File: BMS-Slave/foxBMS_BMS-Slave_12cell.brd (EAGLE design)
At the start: 160 x 100 mm, 371 parts, among them IC1001 ADG728BRUZ, IC1002 ADG728BRUZ, IC1003 LTC6255CS6, IC1004 LTC6255CS6, IC1005 ADG728BRUZ, IC1101 PCA8574TS, IC1201 PCA8574TS, IC1301 24AA02UID, IC1302 MCP9800A0T-M/OT, IC1401 24AA02UID, IC1402 MCP9800A0T-M/OT, IC201 0_LES_BATTERIE-MANAGEMENT.SMD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, IC301 0_LES_BATTERIE-MANAGEMENT.SMD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, IC801 ACPL-247-500E, IC802 ACPL-247-500E, IC803 ACPL-247-500E, IC901 ADG728BRUZ, IC902 ADG728BRUZ, IC903 LTC6255CS6, IC904 LTC6255CS6, IC905 ADG728BRUZ, T201 PBHV8115Z, T301 PBHV8115Z, T701 NX2301P, T702 NX2301P, T703 NX2301P, T704 NX2301P, T705 NX2301P, T706 NX2301P, T707 NX2301P, T708 NX2301P, T709 NX2301P, T710 NX2301P, T711 NX2301P, T712 NX2301P, X1501 MA09-2, X1502 MA09-2, X1503 43045-2400_MOLEX_24PIN, X1504 MA05-2, X1505 MA05-2, X1506 43045-1600_MOLEX_16PIN, X1507 43045-1600_MOLEX_16PIN, X1508 MA10-2, X1509 43045-0200_MOLEX_2PIN, X1510 43045-0200_MOLEX_2PIN, X1511 43045-0200_MOLEX_2PIN, X1512 43045-0200_MOLEX_2PIN

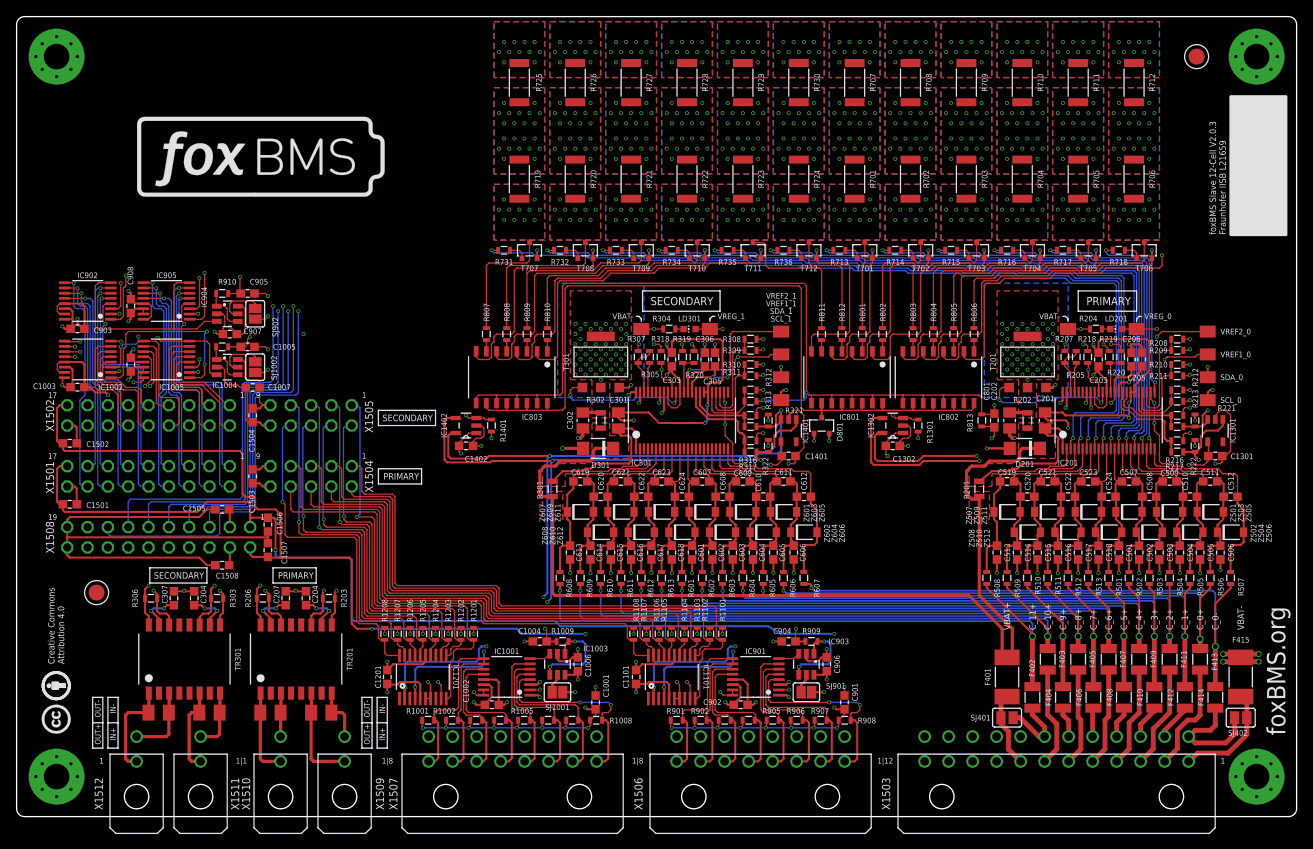
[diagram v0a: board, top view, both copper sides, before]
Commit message: updated foxBMS-slave to version 2.1.0
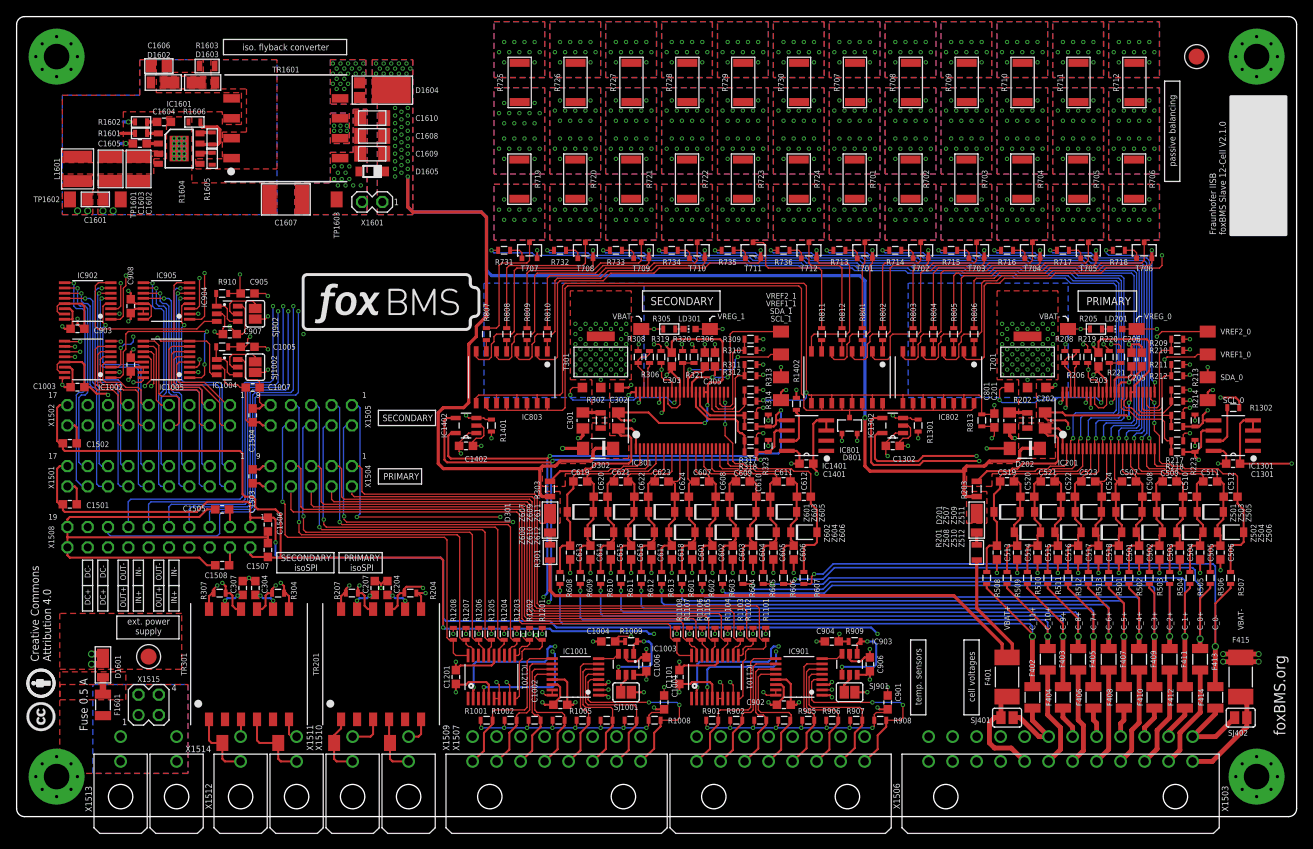
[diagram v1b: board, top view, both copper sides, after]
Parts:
- removed TP202, TP208, TP302, TP308: CUSTOM_PAD_PAD_2.0X1.5MM, foxBMS_BMS-Slave_12cell:CUSTOM_PAD_PAD2.0X1.5MM
- added C1601: 1,00µF_0805_25V_X7R_KEMET, 0_LES_KAPAZITAET.SMD.MLCC:C_SMD_0805_(2012)_R_KEMET_REV01
- added C1602, C1603: 10µF_1210_25V_X7R, 0_LES_KAPAZITAET.SMD.MLCC.KEMET:1210
- added C1604: 100nF, 20%, 16V, foxBMS_BMS-Slave_12cell:C_SMD_0603_(1608)_R_KEMET_REV01
- added C1605: 1uF, 20%, 16V, foxBMS_BMS-Slave_12cell:C_SMD_0603_(1608)_R_KEMET_REV01
- added C1606: 470PF_0805_50V_X7R_KEMET, 0_LES_KAPAZITAET.SMD.MLCC:C_SMD_0805_(2012)_R_KEMET_REV01
- added C1607: 4,7NF_1812, 0_LES_KAPAZITAET.SMD.MLCC.KEMET_custom:1812
- added C1608, C1609, C1610: 4,70µF_1206_25V_X7R_KEMET, 0_LES_KAPAZITAET.SMD.MLCC:C_SMD_1206_(3216)_R_KEMET_REV01
- added D1601, D1603: DI_DFLS1100, diodes_custom:POWER_DI_123
- added D1602: DI_DFLZ36, diodes_custom:POWER_DI_123
- added D1604: DI_PDS3200, diodes_custom:POWER_DI_5
- added D1605: MMSZ5263B, L21596_V1.0:SOD123
- added D202, D302: SMAJ60CA_VISHAY, foxBMS_BMS-Slave_12cell:D_SMD_SMA_(DO-214AC)_(BIDIR)_R_VISHAY_REV01
- added F1601: 1,250A_LITTELFUSE_466_1206, foxBMS_BMS-Slave_12cell:R_SMD_CHIP_1206_R_LITTLEFUSE_REV_01
- added IC1601: LT8302, linear_custom:S8E
- added L1601: WE-74404042100, inductor_custom:WE-LQS
- added R1302, R1402: 10,0K_0603_R_VISHAY_1%_TK100_REV_01, foxBMS_BMS-Slave_12cell:R_SMD_0603_R_VISHAY_REV01
- added R1601: 390K_0603_R_VISHAY_1%_TK100_REV_01, 0_LES_WIDERSTAND.SMD.CHIP.DICKSCHICHT:R_SMD_0603_R_VISHAY_REV01
- added R1602: 86,6K_0603_R_VISHAY_1%_TK100_REV_01, 0_LES_WIDERSTAND.SMD.CHIP.DICKSCHICHT:R_SMD_0603_R_VISHAY_REV01
- added R1603: 39,0R_0805_R_VISHAY_1%_TK100_REV_01, 0_LES_WIDERSTAND.SMD.CHIP.DICKSCHICHT:R_SMD_0805_R_VISHAY_REV01
- added R1604: DUMMY_R_CHIP_0603_R_VISHAY, 0_LES_WIDERSTAND.SMD.CHIP.DICKSCHICHT:R_SMD_0603_R_VISHAY_REV01
- added R1605: 127K_0603_R_VISHAY_1%_TK100_REV_01, 0_LES_WIDERSTAND.SMD.CHIP.DICKSCHICHT:R_SMD_0603_R_VISHAY_REV01
- added R1606: 10,0K_0603_R_VISHAY_1%_TK100_REV_01, 0_LES_WIDERSTAND.SMD.CHIP.DICKSCHICHT:R_SMD_0603_R_VISHAY_REV01
- added R223, R323: 1.2k, 10%, 1/10W, foxBMS_BMS-Slave_12cell:R_SMD_0603_R_VISHAY_REV01
- added TP1601, TP1602, TP1603: CUSTOM_PAD_PAD_2.0X1.5MM, foxBMS_BMS-Slave_12cell:CUSTOM_PAD_PAD2.0X1.5MM
- added TR1601: WE_750313457, transformer_custom:WUERTH_CUSTOM
- added X1513, X1514: 43045-0200_MOLEX_2PIN, foxBMS_BMS-Slave_12cell:X_TH_MOLEX_43045-0200_R_REV01
- added X1515: MA02-2_TH, custom_connector:MA02-2
- added X1601: MA02-1_TH, custom_connector:MA02-1A
- D201, D301: value SMAJ60CA_VISHAY -> DI_DFLS1100; device foxBMS_BMS-Slave_12cell:D_SMD_SMA_(DO-214AC)_(BIDIR)_R_VISHAY_REV01 -> diodes_custom:POWER_DI_123
- IC1301, IC1401: value 24AA02UID -> M24M02-DR; device foxBMS_BMS-Slave_12cell:IC_SMD_SOT23-5_R_MICROCHIP_REV01 -> eeprom_custom:SOIC127P600X175-8N
- R201, R301: value 100R, 1%, 1/10W -> 0,00R_0805_R_VISHAY_REV_01; device foxBMS_BMS-Slave_12cell:R_SMD_0805_R_VISHAY_REV01 -> 0_LES_WIDERSTAND.SMD.CHIP.DICKSCHICHT:R_SMD_0805_R_VISHAY_REV01
- R203, R303: value 120R, 1%, 1/10W -> 100R, 1%, 1/10W; device foxBMS_BMS-Slave_12cell:R_SMD_0603_R_VISHAY_REV01 -> foxBMS_BMS-Slave_12cell:R_SMD_0805_R_VISHAY_REV01
- R204, R304: value 270R, 1%, 1/10W -> 120R, 1%, 1/10W
- R205, R305: value 820R, 1%, 1/10W -> 330R, 1%, 1/10W; device foxBMS_BMS-Slave_12cell:R_SMD_0603_R_VISHAY_REV01 -> 0_LES_WIDERSTAND.SMD.CHIP.DICKSCHICHT:R_SMD_0603_R_VISHAY_REV01
- R206, R306: value 120R, 1%, 1/10W -> 820R, 1%, 1/10W
- R207, R307: value 1.21k, 1%, 1/10W -> 120R, 1%, 1/10W
- R208, R308: value OPT -> 1.21k, 1%, 1/10W
- R209, R211, R213, R215, R217, R309, R311, R313, R315, R317: value 0R -> OPT
- R210, R212, R214, R216, R220, R310, R312, R314, R316, R320: value OPT -> 0R
- R218, R318: value 1M, 10%, 1/10W -> 0R
- R219, R319: value 0R -> 1M, 10%, 1/10W
- R221, R321: value 1.2k, 10%, 1/10W -> OPT
- R701, R702, R703, R704, R705, R706, R707, R708, R709, R710, R711, R712, R719, R720, R721, R722, R723, R724, R725, R726, R727, R728, R729, R730: value 18R, 1%, 0.4W -> 72R, 1%; device foxBMS_BMS-Slave_12cell:R_SMD_2010_R_YAGEO_REV01 -> 0_LES_WIDERSTAND.SMD.CHIP.DICKSCHICHT:R_SMD_2010_R_YAGEO_REV01
- TR201, TR301: value HX1188NL -> HM2102NL; device foxBMS_BMS-Slave_12cell:TR_SMD_SOIC-16_(12,70MMX9,53MMX5,97MM)_R_PULSE_REV01 -> transformer_custom:HM2102NL
- moved R206 106.1 mm to (132.5, 57.5), turned to 270 degrees
- moved R207 93.9 mm to (41.9, 27.9), turned to 0 degrees
- moved R204 91.8 mm to (49.2, 27.9)
- moved R203 82.1 mm to (120.0, 41.0), turned to 90 degrees
- moved R306 69.2 mm to (79.1, 57.5), turned to 270 degrees
- moved R307 60.1 mm to (25.4, 27.9), turned to 0 degrees
- moved R304 59.0 mm to (32.7, 27.9)
- moved R303 43.8 mm to (66.7, 41.0), turned to 90 degrees
- moved R318 16.3 mm to (91.7, 45.6), turned to 180 degrees
- moved R218 16.3 mm to (145.1, 45.6), turned to 180 degrees
- moved R208 14.2 mm to (131.0, 57.5), turned to 270 degrees
- moved R308 14.2 mm to (77.7, 57.5), turned to 270 degrees
- moved X1512 13.0 mm to (28.0, 2.50)
- moved R221 12.2 mm to (138.0, 57.5)
- moved R321 12.2 mm to (84.7, 57.5)
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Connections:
- removed net N$11: R705.P$1, R711.P$2
- removed net N$13: R704.P$1, R710.P$2
- removed net N$19: R703.P$1, R709.P$2
- removed net N$21: R701.P$1, R707.P$2
- removed net N$23: R702.P$1, R708.P$2
- removed net N$27: R719.P$1, R725.P$2
- removed net N$29: R720.P$1, R726.P$2
- removed net N$4: R706.P$1, R712.P$2
- removed net N$41: R721.P$1, R727.P$2
- removed net N$43: R722.P$1, R728.P$2
- removed net N$46: R723.P$1, R729.P$2
- removed net N$48: R724.P$1, R730.P$2
- new net EXT_DC_IN+: F1601.P$1, X1513.1, X1514.1, X1515.1, X1515.3
- new net EXT_DC_IN-: C1601.P$1, C1602.P$1, C1603.P$1, C1604.1, C1605.1, C1607.P$1, IC1601.4, IC1601.P$1, R1602.1, R1606.1, TP1601.P$1, X1513.2, X1514.2, X1515.2, X1515.4
- new net EXT_DC_ISO+: C1608.P$2, C1609.P$2, C1610.P$2, D1604.K, D1605.C, D201.K, D202.C, D301.K, D302.C, R202.2, R203.1, R302.2, R303.1, X1601.1
- new net N$1254: C1602.P$2, C1603.P$2, C1606.P$2, D1602.A, IC1601.3, L1601.2, R1601.2, TR1601.3, TR1601.4
- new net N$68: C1604.2, IC1601.1, R1601.1, R1602.2
- new net N$71: C1605.2, IC1601.2
- new net N$74: TR1601.6, TR1601.7
- new net N$76: D201.A, R201.2
- new net N$77: IC1601.7, R1604.2, R1606.2
- new net N$79: IC1601.6, R1605.1
- new net N$80: D1603.A, IC1601.5, R1603.1, R1605.2, TR1601.1, TR1601.2
- new net N$82: IC1601.8, R1604.1
- new net N$84: D1604.A1, D1604.A2, TR1601.5
- new net N$87: C1606.P$1, R1603.2
- new net N$89: D1601.A, F1601.P$2
- new net N$91: C1601.P$2, D1601.K, L1601.1, TP1602.P$1
- new net N$92: D1602.K, D1603.K
- new net N$94: IC1301.7, R1302.1
- new net N$95: IC1401.7, R1402.1
- new net N$96: D301.A, R301.2
- net +5.0V_VREG_0: now also IC1301.8, R1302.2, R219.2, R223.2; no longer IC1301.4, R218.2, R220.2
- net +5.0V_VREG_1: now also IC1401.8, R1402.2, R319.2, R323.2; no longer IC1401.4, R318.2, R320.2
- net CELL0_FEEDBACK+: now also R712.P$2
- net CELL10_FEEDBACK+: now also R726.P$2
- net CELL11_FEEDBACK+: now also R725.P$2
- net CELL1_FEEDBACK+: now also R711.P$2
- net CELL2_FEEDBACK+: now also R710.P$2
- net CELL3_FEEDBACK+: now also R709.P$2
- net CELL4_FEEDBACK+: now also R708.P$2
- net CELL5_FEEDBACK+: now also R707.P$2
- net CELL6_FEEDBACK+: now also R730.P$2
- net CELL7_FEEDBACK+: now also R729.P$2
- net CELL8_FEEDBACK+: now also R728.P$2
- net CELL9_FEEDBACK+: now also R727.P$2
- net FUSED_CELL_0+: now also R705.P$1
- net FUSED_CELL_0-: now also R706.P$1
- net FUSED_CELL_1+: now also R704.P$1
- net FUSED_CELL_10+: now also R719.P$1
- net FUSED_CELL_2+: now also R703.P$1
- net FUSED_CELL_3+: now also R702.P$1
- net FUSED_CELL_4+: now also R701.P$1
- net FUSED_CELL_5+: now also R724.P$1
- net FUSED_CELL_6+: now also R723.P$1
- net FUSED_CELL_7+: now also R722.P$1
- net FUSED_CELL_8+: now also R721.P$1
- net FUSED_CELL_9+: now also R720.P$1
- net FUSED_VBAT+: no longer D201.C, D301.C, R202.2, R302.2
- net FUSED_VBAT-: now also C1607.P$2, C1608.P$1, C1609.P$1, C1610.P$1, D1605.A, D202.A, D302.A, IC1301.3, IC1301.4, IC1401.3, IC1401.4, R205.1, R208.1, R220.1, R305.1, R308.1, R320.1, TP1603.P$1, TR1601.8, X1601.2; no longer D201.A, D301.A, IC1301.2, IC1401.2, R204.1, R207.1, R219.1, R304.1, R307.1, R319.1
- net GLOBAL-BALANCING-FEEDBACK: now also R214.1, R314.1; no longer R213.1, R313.1
- net N$12: now also R206.2; no longer R205.2
- net N$14: now also TR301.11; no longer TR301.15
- net N$15: now also TR301.8; no longer TR301.10
- net N$17: now also C202.P$1, R203.2; no longer C201.P$1, R201.2
- net N$24: now also C302.P$1, R303.2; no longer C301.P$1, R301.2
- net N$25: now also C301.P$1; no longer C302.P$1
- net N$33: now also R306.2; no longer R305.2
- net N$34: now also R205.2; no longer R204.2
- net N$38: now also R305.2; no longer R304.2
- net N$40: now also R316.2; no longer R314.2
- net N$5: now also TR201.11; no longer TR201.15
- net N$7: now also C201.P$1; no longer C202.P$1
- net N$9: now also TR201.8; no longer TR201.10
- net PRIMARY-GPIO0: now also R210.2; no longer R208.2
- net PRIMARY-GPIO1: now also R212.2; no longer R210.2
- net PRIMARY-GPIO1-OPT: now also R209.1; no longer R208.1
- net PRIMARY-GPIO2-OPT: now also R211.1; no longer R210.1
- net PRIMARY-GPIO3: now also R216.2; no longer R214.2
- net PRIMARY-GPIO3-OPT: now also R213.1; no longer R212.1
- net PRIMARY-GPIO4: now also R218.2; no longer R216.2
- net PRIMARY-GPIO4-OPT: now also R215.1; no longer R214.1
- net PRIMARY-GPIO5: now also R214.2; no longer R212.2
- net PRIMARY-GPIO5-OPT: now also R217.1; no longer R216.1
- net PRIMARY-ICMP: now also R206.1, R208.2; no longer R205.1, R207.2
- net PRIMARY-ICMP1: now also R306.1, R308.2; no longer R305.1, R307.2
- net PRIMARY-IN+: now also TR201.4; no longer TR201.6
- net PRIMARY-IN-: now also TR201.6; no longer TP202.P$1, TR201.8
- net PRIMARY-IN_N1: now also R204.2, TR201.7; no longer R203.2, TR201.9
- net PRIMARY-IN_P1: now also R204.1, TR201.9; no longer R203.1, TR201.11
- net PRIMARY-MUX-DATA_TEMP: now also R210.1; no longer R209.1
- net PRIMARY-MUX-DATA_USER: now also R212.1; no longer R211.1
- net PRIMARY-OUT-: no longer TP208.P$1
- net PRIMARY-OUT_N1: now also R207.2, TR201.10; no longer R206.2, TR201.14
- net PRIMARY-OUT_P1: now also R207.1, TR201.12; no longer R206.1, TR201.16
- net PRIMARY-SCL_0: now also IC1301.6, R218.1, R223.1; no longer IC1301.1, R217.1, R222.1
- net PRIMARY-SDA_0: now also IC1301.5, R216.1, R222.1; no longer IC1301.3, R215.1, R221.1
- net PRIMARY-SWTEN: now also R220.2, R221.1; no longer R219.2, R220.1
- net PRIMARY-SWTEN1: now also R320.2, R321.1; no longer R319.2, R320.1
- net PRIMARY-WDT: now also R219.1; no longer R218.1
- net SECONDARY-GPIO0: now also R310.2; no longer R308.2
- net SECONDARY-GPIO1: now also R312.2; no longer R310.2
- net SECONDARY-GPIO1-OPT: now also R309.1; no longer R308.1
- net SECONDARY-GPIO2-OPT: now also R311.1; no longer R310.1
- net SECONDARY-GPIO3-OPT: now also R313.1; no longer R312.1
- net SECONDARY-GPIO4: now also R318.2; no longer R316.2
- net SECONDARY-GPIO4-OPT: now also R315.1; no longer R314.1
- net SECONDARY-GPIO5: now also R314.2; no longer R312.2
- net SECONDARY-GPIO5-OPT: now also R317.1; no longer R316.1
- net SECONDARY-IN+: now also TR301.4; no longer TR301.6
- net SECONDARY-IN-: now also TR301.6; no longer TP302.P$1, TR301.8
- net SECONDARY-IN_N1: now also R304.2, TR301.7; no longer R303.2, TR301.9
- net SECONDARY-IN_P1: now also R304.1, TR301.9; no longer R303.1, TR301.11
- net SECONDARY-MUX-DATA_TEMP: now also R310.1; no longer R309.1
- net SECONDARY-MUX-DATA_USER: now also R312.1; no longer R311.1
- net SECONDARY-OUT-: no longer TP308.P$1
- net SECONDARY-OUT_N1: now also R307.2, TR301.10; no longer R306.2, TR301.14
- net SECONDARY-OUT_P1: now also R307.1, TR301.12; no longer R306.1, TR301.16
- net SECONDARY-SCL_1: now also IC1401.6, R318.1, R323.1; no longer IC1401.1, R317.1, R322.1
- net SECONDARY-SDA_1: now also IC1401.5, R316.1, R322.1; no longer IC1401.3, R315.1, R321.1
- net SECONDARY-WDT: now also R319.1; no longer R318.1
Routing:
- net EXT_DC_ISO+: track 0.00 -> 199.1 mm, vias 0 -> 45
- net EXT_DC_IN-: track 0.00 -> 90.6 mm, vias 0 -> 19
- net N$91: track 0.00 -> 78.5 mm, vias 0 -> 4
- net FUSED_VBAT+: track 128.2 -> 79.3 mm
- net FUSED_CELL_8+: track 309.5 -> 279.5 mm, vias 14 -> 25
- net FUSED_CELL_7+: track 310.3 -> 280.4 mm, vias 14 -> 25
- net FUSED_CELL_6+: track 277.3 -> 247.4 mm, vias 14 -> 25
- net FUSED_CELL_9+: track 318.7 -> 288.8 mm, vias 14 -> 25
- net FUSED_CELL_10+: track 318.5 -> 288.6 mm, vias 14 -> 25
- net FUSED_CELL_5+: track 267.7 -> 242.0 mm, vias 14 -> 25
- net FUSED_CELL_4+: track 258.4 -> 234.4 mm, vias 14 -> 25
- net FUSED_CELL_3+: track 258.8 -> 237.8 mm, vias 14 -> 25
- net FUSED_CELL_2+: track 248.3 -> 227.6 mm, vias 14 -> 25
- net FUSED_CELL_1+: track 248.9 -> 228.5 mm, vias 14 -> 25
- net CELL1_FEEDBACK+: track 26.4 -> 45.6 mm, vias 11 -> 22
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- added copper zone on layer 16, net CELL0_FEEDBACK+1
- added copper zone on layer 16, net CELL10_FEEDBACK+1
- added copper zone on layer 16, net CELL11_FEEDBACK+1
- added copper zone on layer 16, net CELL1_FEEDBACK+1
- added copper zone on layer 16, net CELL2_FEEDBACK+1
- added copper zone on layer 16, net CELL3_FEEDBACK+1
- added copper zone on layer 16, net CELL4_FEEDBACK+1
- added copper zone on layer 16, net CELL5_FEEDBACK+1
- added copper zone on layer 16, net CELL6_FEEDBACK+1
- added copper zone on layer 16, net CELL7_FEEDBACK+1
- added copper zone on layer 16, net CELL8_FEEDBACK+1
- added copper zone on layer 16, net CELL9_FEEDBACK+1
- added copper zone on layer 1, net EXT_DC_IN+
- added copper zone on layer 1, net EXT_DC_IN-
- added copper zone on layer 16, net EXT_DC_IN-
- added copper zone on layer 1, net EXT_DC_ISO+
- added copper zone on layer 16, net EXT_DC_ISO+
- added copper zone on layer 1, net FUSED_VBAT-
- added copper zone on layer 16, net FUSED_VBAT-
- added copper zone on layer 1, net N$1254
- added copper zone on layer 1, net N$74
- added copper zone on layer 16, net N$74
- added copper zone on layer 1, net N$80
- added copper zone on layer 1, net N$84
- added copper zone on layer 16, net N$84
- added copper zone on layer 1, net N$87
- added copper zone on layer 1, net N$89
- added copper zone on layer 1, net N$91
- added copper zone on layer 1, net N$92
- removed copper zone on layer 16, net FUSED_CELL_0+
- removed copper zone on layer 16, net FUSED_CELL_0-
- removed copper zone on layer 16, net FUSED_CELL_1+
- removed copper zone on layer 16, net FUSED_CELL_10+
- removed copper zone on layer 16, net FUSED_CELL_2+
- removed copper zone on layer 16, net FUSED_CELL_3+
- removed copper zone on layer 16, net FUSED_CELL_4+
- removed copper zone on layer 16, net FUSED_CELL_5+
- removed copper zone on layer 16, net FUSED_CELL_6+
- removed copper zone on layer 16, net FUSED_CELL_7+
- removed copper zone on layer 16, net FUSED_CELL_8+
- removed copper zone on layer 16, net FUSED_CELL_9+
- removed copper zone on layer 1, net FUSED_VBAT+
- removed copper zone on layer 1, net N$11
- removed copper zone on layer 1, net N$13
- removed copper zone on layer 1, net N$19
- removed copper zone on layer 1, net N$21
- removed copper zone on layer 1, net N$23
- removed copper zone on layer 1, net N$27
- removed copper zone on layer 1, net N$29
- removed copper zone on layer 1, net N$4
- removed copper zone on layer 1, net N$41
- removed copper zone on layer 1, net N$43
- removed copper zone on layer 1, net N$46
- removed copper zone on layer 1, net N$48
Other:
- board text added: "DC+"
- board text added: "DC-"
- board text added: "Fraunhofer IISB foxBMS Slave 12-Cell V2.1.0"
- board text added: "Fuse 0.5 A"
- board text added: "PRIMARY isoSPI"
- board text added: "SECONDARY isoSPI"
- board text added: "TP1601"
- board text added: "TP1602"
- board text added: "TP1603"
- board text added: "cell voltages"
- board text added: "ext. power supply"
- board text added: "iso. flyback converter"
- board text added: "passive balancing"
- board text added: "temp. sensors"
- board text removed: "1"
- board text removed: "1|1"
- board text removed: "1|12"
- board text removed: "1|8"
- board text removed: "foxBMS Slave 12-Cell V2.0.3 Fraunhofer IISB L21659"
